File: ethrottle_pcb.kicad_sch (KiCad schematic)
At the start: 57 parts, among them J1 ATM15-08PA-BM02, Q1 ZXTR2105F-7, U1 MCP6004, U2 MCP6004, U3 MCP6004, U4 UB2-5NUN

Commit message: finished routing
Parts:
- H1, H2, H3, H4: footprint (none) -> MountingHole:MountingHole_3.5mm_Pad
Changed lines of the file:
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@@
       (effects (font (size 1.27 1.27)) (justify left))
     )
-    (property "Footprint" "" (id 2) (at 241.3 27.94 0)
+    (property "Footprint" "MountingHole:MountingHole_3.5mm_Pad" (id 2) (at 241.3 27.94 0)
       (effects (font (size 1.27 1.27)) hide)
     )
@@
       (effects (font (size 1.27 1.27)) (justify left))
     )
-    (property "Footprint" "" (id 2) (at 237.49 27.94 0)
+    (property "Footprint" "MountingHole:MountingHole_3.5mm_Pad" (id 2) (at 237.49 27.94 0)
       (effects (font (size 1.27 1.27)) hide)
     )
@@
       (effects (font (size 1.27 1.27)) (justify left))
     )
-    (property "Footprint" "" (id 2) (at 233.68 27.94 0)
+    (property "Footprint" "MountingHole:MountingHole_3.5mm_Pad" (id 2) (at 233.68 27.94 0)
       (effects (font (size 1.27 1.27)) hide)
     )
@@
       (effects (font (size 1.27 1.27)) (justify left))
     )
-    (property "Footprint" "" (id 2) (at 245.11 27.94 0)
+    (property "Footprint" "MountingHole:MountingHole_3.5mm_Pad" (id 2) (at 245.11 27.94 0)
       (effects (font (size 1.27 1.27)) hide)
     )
@@
     )
     (path "/c86d50f5-711f-4a3c-a410-cabcde07bdde"
-      (reference "H1") (unit 1) (value "MountingHole_Pad") (footprint "")
+      (reference "H1") (unit 1) (value "MountingHole_Pad") (footprint "MountingHole:MountingHole_3.5mm_Pad")
     )
     (path "/9a5cb1a6-f24b-4474-afa2-0fecffe0198e"
-      (reference "H2") (unit 1) (value "MountingHole_Pad") (footprint "")
+      (reference "H2") (unit 1) (value "MountingHole_Pad") (footprint "MountingHole:MountingHole_3.5mm_Pad")
     )
     (path "/47b0c02d-82c1-43cd-8381-8e6ee286c3ef"
-      (reference "H3") (unit 1) (value "MountingHole_Pad") (footprint "")
+      (reference "H3") (unit 1) (value "MountingHole_Pad") (footprint "MountingHole:MountingHole_3.5mm_Pad")
     )
     (path "/e2c40712-e7d7-45b4-872b-410fde8473b9"
-      (reference "H4") (unit 1) (value "MountingHole_Pad") (footprint "")
+      (reference "H4") (unit 1) (value "MountingHole_Pad") (footprint "MountingHole:MountingHole_3.5mm_Pad")
     )
     (path "/4f0316f3-2f03-4993-a8a1-815407511b62"

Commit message: layout edits
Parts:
- added TP1: TREF-Test, TestPoint:TestPoint_Plated_Hole_D2.0mm, symbol Connector:TestPoint
- added TP2: BREF-Test, TestPoint:TestPoint_Plated_Hole_D2.0mm, symbol Connector:TestPoint
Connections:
- net BREF: now also TP2.1
- net TREF: now also TP1.1
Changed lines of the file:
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@@
   (junction (at 62.23 66.04) (diameter 0) (color 0 0 0 0)
   )
+  (junction (at 69.85 52.07) (diameter 0) (color 0 0 0 0)
+  )
+  (junction (at 69.85 71.12) (diameter 0) (color 0 0 0 0)
+  )
   (wire (pts (xy 160.02 60.96) (xy 166.37 60.96))
     (stroke (width 0) (type default) (color 0 0 0 0))
@@
     (stroke (width 0) (type default) (color 0 0 0 0))
   )
+  (wire (pts (xy 64.77 66.04) (xy 73.66 66.04))
+    (stroke (width 0) (type default) (color 0 0 0 0))
+  )
   (wire (pts (xy 100.33 90.17) (xy 114.3 90.17))
     (stroke (width 0) (type default) (color 0 0 0 0))
@@
     (stroke (width 0) (type default) (color 0 0 0 0))
   )
+  (wire (pts (xy 59.69 71.12) (xy 69.85 71.12))
+    (stroke (width 0) (type default) (color 0 0 0 0))
+  )
   (wire (pts (xy 270.51 93.98) (xy 270.51 86.36))
     (stroke (width 0) (type default) (color 0 0 0 0))
@@
     (stroke (width 0) (type default) (color 0 0 0 0))
   )
+  (wire (pts (xy 69.85 52.07) (xy 73.66 52.07))
+    (stroke (width 0) (type default) (color 0 0 0 0))
+  )
   (wire (pts (xy 59.69 66.04) (xy 62.23 66.04))
     (stroke (width 0) (type default) (color 0 0 0 0))
@@
     (stroke (width 0) (type default) (color 0 0 0 0))
   )
-  (wire (pts (xy 64.77 66.04) (xy 73.66 66.04))
-    (stroke (width 0) (type default) (color 0 0 0 0))
-  )
   (wire (pts (xy 222.25 99.06) (xy 227.33 99.06))
     (stroke (width 0) (type default) (color 0 0 0 0))
   )
+  (wire (pts (xy 64.77 52.07) (xy 69.85 52.07))
+    (stroke (width 0) (type default) (color 0 0 0 0))
+  )
   (wire (pts (xy 271.78 101.6) (xy 267.97 101.6))
     (stroke (width 0) (type default) (color 0 0 0 0))
@@
   )
   (wire (pts (xy 223.52 113.03) (xy 271.78 113.03))
+    (stroke (width 0) (type default) (color 0 0 0 0))
+  )
+  (wire (pts (xy 69.85 71.12) (xy 73.66 71.12))
     (stroke (width 0) (type default) (color 0 0 0 0))
   )
@@
     )
   )
-  (global_label "BREF" (shape input) (at 73.66 71.12 180) (fields_autoplaced)
+  (global_label "BREF" (shape input) (at 59.69 71.12 180) (fields_autoplaced)
     (effects (font (size 1.27 1.27)) (justify right))
-    (property "Intersheet References" "${INTERSHEET_REFS}" (id 0) (at 66.4693 71.1994 0)
+    (property "Intersheet References" "${INTERSHEET_REFS}" (id 0) (at 52.4993 71.1994 0)
       (effects (font (size 1.27 1.27)) (justify right) hide)
     )
@@
     )
   )
-  (global_label "TREF" (shape input) (at 73.66 52.07 180) (fields_autoplaced)
+  (global_label "TREF" (shape input) (at 64.77 52.07 180) (fields_autoplaced)
     (effects (font (size 1.27 1.27)) (justify right))
-    (property "Intersheet References" "${INTERSHEET_REFS}" (id 0) (at 66.7717 52.1494 0)
+    (property "Intersheet References" "${INTERSHEET_REFS}" (id 0) (at 57.8817 52.1494 0)
       (effects (font (size 1.27 1.27)) (justify right) hide)
     )
@@
     (pin "1")
   )
+  (symbol (lib_id "Connector:TestPoint") (at 69.85 52.07 180) (unit 1)
+    (in_bom yes) (on_board yes)
+    (property "Reference" "TP1" (id 0) (at 69.85 49.53 0)
+      (effects (font (size 1.27 1.27)) (justify right))
+    )
+    (property "Value" "TREF-Test" (id 1) (at 72.39 63.5 90)
+      (effects (font (size 1.27 1.27)) (justify right))
+    )
+    (property "Footprint" "TestPoint:TestPoint_Plated_Hole_D2.0mm" (id 2) (at 64.77 52.07 0)
+      (effects (font (size 1.27 1.27)) hide)
+    )
+    (property "Datasheet" "~" (id 3) (at 64.77 52.07 0)
+      (effects (font (size 1.27 1.27)) hide)
+    )
+    (pin "1")
+  )
   (symbol (lib_id "Amplifier_Operational:MCP6004") (at 214.63 143.51 0) (unit 5)
     (in_bom yes) (on_board yes)
@@
     (pin "1")
   )
+  (symbol (lib_id "Connector:TestPoint") (at 69.85 71.12 180) (unit 1)
+    (in_bom yes) (on_board yes)
+    (property "Reference" "TP2" (id 0) (at 71.12 73.66 0)
+      (effects (font (size 1.27 1.27)) (justify right))
+    )
+    (property "Value" "BREF-Test" (id 1) (at 72.39 85.09 90)
+      (effects (font (size 1.27 1.27)) (justify right))
+    )
+    (property "Footprint" "TestPoint:TestPoint_Plated_Hole_D2.0mm" (id 2) (at 64.77 71.12 0)
+      (effects (font (size 1.27 1.27)) hide)
+    )
+    (property "Datasheet" "~" (id 3) (at 64.77 71.12 0)
+      (effects (font (size 1.27 1.27)) hide)
+    )
+    (pin "1")
+  )
   (symbol (lib_id "power:GND") (at 179.07 151.13 0) (unit 1)
     (in_bom yes) (on_board yes) (fields_autoplaced)
@@
       (reference "R26") (unit 1) (value "1k") (footprint "Resistor_SMD:R_01005_0402Metric")
     )
+    (path "/0f398a6b-70fb-4a4d-8c4d-409df7e390fd"
+      (reference "TP1") (unit 1) (value "TREF-Test") (footprint "TestPoint:TestPoint_Plated_Hole_D2.0mm")
+    )
+    (path "/3a6f3c75-f7a5-4176-9d15-a707551bc0d9"
+      (reference "TP2") (unit 1) (value "BREF-Test") (footprint "TestPoint:TestPoint_Plated_Hole_D2.0mm")
+    )
     (path "/f0df9610-d7e0-45ea-82a7-3deb1fb5d694"

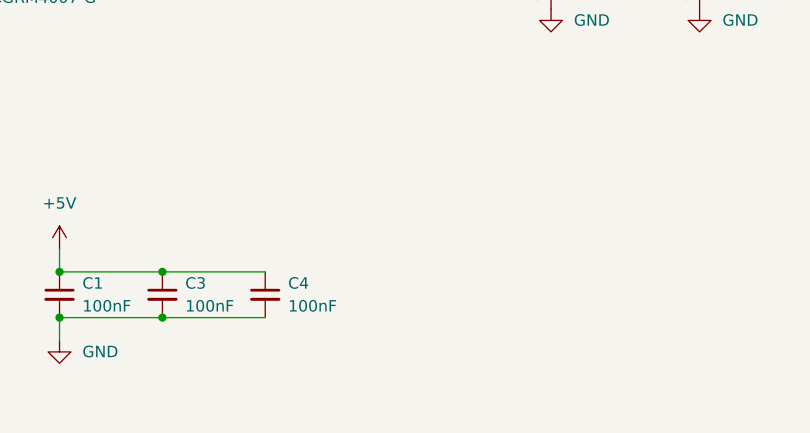
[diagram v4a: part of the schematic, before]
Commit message: add decoupling capacitor
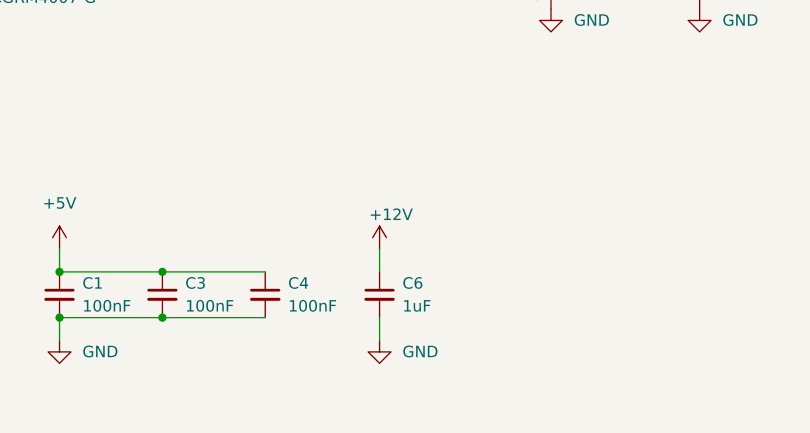
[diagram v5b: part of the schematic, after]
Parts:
- added C6: 1uF, Capacitor_SMD:C_0201_0603Metric, symbol Device:C_Small
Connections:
- net +12V: now also C6.1
- net GND: now also C6.2
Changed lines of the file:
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@@
+    (stroke (width 0) (type default) (color 0 0 0 0))
+  )
+  (wire (pts (xy 160.02 185.42) (xy 160.02 187.96))
     (stroke (width 0) (type default) (color 0 0 0 0))
   )
@@
   )
   (wire (pts (xy 57.15 133.35) (xy 62.23 133.35))
+    (stroke (width 0) (type default) (color 0 0 0 0))
+  )
+  (wire (pts (xy 160.02 177.8) (xy 160.02 180.34))
     (stroke (width 0) (type default) (color 0 0 0 0))
   )
@@
     (pin "2")
   )
+  (symbol (lib_id "power:GND") (at 160.02 187.96 0) (unit 1)
+    (in_bom yes) (on_board yes) (fields_autoplaced)
+    (property "Reference" "#PWR051" (id 0) (at 160.02 194.31 0)
+      (effects (font (size 1.27 1.27)) hide)
+    )
+    (property "Value" "GND" (id 1) (at 162.56 189.2299 0)
+      (effects (font (size 1.27 1.27)) (justify left))
+    )
+    (property "Footprint" "" (id 2) (at 160.02 187.96 0)
+      (effects (font (size 1.27 1.27)) hide)
+    )
+    (property "Datasheet" "" (id 3) (at 160.02 187.96 0)
+      (effects (font (size 1.27 1.27)) hide)
+    )
+    (pin "1")
+  )
   (symbol (lib_id "power:GND") (at 124.46 187.96 0) (unit 1)
     (in_bom yes) (on_board yes) (fields_autoplaced)
@@
     (pin "1")
     (pin "2")
+  )
+  (symbol (lib_id "power:+12V") (at 160.02 177.8 0) (unit 1)
+    (in_bom yes) (on_board yes)
+    (property "Reference" "#PWR050" (id 0) (at 160.02 181.61 0)
+      (effects (font (size 1.27 1.27)) hide)
+    )
+    (property "Value" "+12V" (id 1) (at 161.29 173.99 0))
+    (property "Footprint" "" (id 2) (at 160.02 177.8 0)
+      (effects (font (size 1.27 1.27)) hide)
+    )
+    (property "Datasheet" "" (id 3) (at 160.02 177.8 0)
+      (effects (font (size 1.27 1.27)) hide)
+    )
+    (pin "1")
   )
   (symbol (lib_id "power:PWR_FLAG") (at 97.79 182.88 0) (unit 1)
@@
     (pin "2")
   )
+  (symbol (lib_id "Device:C_Small") (at 160.02 182.88 0) (unit 1)
+    (in_bom yes) (on_board yes) (fields_autoplaced)
+    (property "Reference" "C6" (id 0) (at 162.56 181.6162 0)
+      (effects (font (size 1.27 1.27)) (justify left))
+    )
+    (property "Value" "1uF" (id 1) (at 162.56 184.1562 0)
+      (effects (font (size 1.27 1.27)) (justify left))
+    )
+    (property "Footprint" "Capacitor_SMD:C_0201_0603Metric" (id 2) (at 160.02 182.88 0)
+      (effects (font (size 1.27 1.27)) hide)
+    )
+    (property "Datasheet" "https://search.murata.co.jp/Ceramy/image/img/A01X/G101/ENG/GRM033R60J105MEA2-02.pdf" (id 3) (at 160.02 182.88 0)
+      (effects (font (size 1.27 1.27)) hide)
+    )
+    (pin "1")
+    (pin "2")
+  )
   (symbol (lib_id "Amplifier_Operational:MCP6004") (at 173.99 58.42 0) (unit 2)
     (in_bom yes) (on_board yes) (fields_autoplaced)
@@
       (reference "#PWR049") (unit 1) (value "+12V") (footprint "")
     )
+    (path "/3e99151b-271e-4b50-af12-3cf637629ce9"
+      (reference "#PWR050") (unit 1) (value "+12V") (footprint "")
+    )
+    (path "/32e28533-9f5b-4d98-8a95-d6c101584a0e"
+      (reference "#PWR051") (unit 1) (value "GND") (footprint "")
+    )
     (path "/1b640f29-3d5f-434a-b351-9c2d1cc03452"
       (reference "C1") (unit 1) (value "100nF") (footprint "Capacitor_SMD:C_0201_0603Metric")
@@
       (reference "C5") (unit 1) (value "10uF") (footprint "Capacitor_SMD:C_0805_2012Metric")
     )
+    (path "/bd515c98-1462-4b1d-bef4-56a57db1aee7"
+      (reference "C6") (unit 1) (value "1uF") (footprint "Capacitor_SMD:C_0201_0603Metric")
+    )
     (path "/cd943169-25c5-42dc-b71b-d2aa00184062"

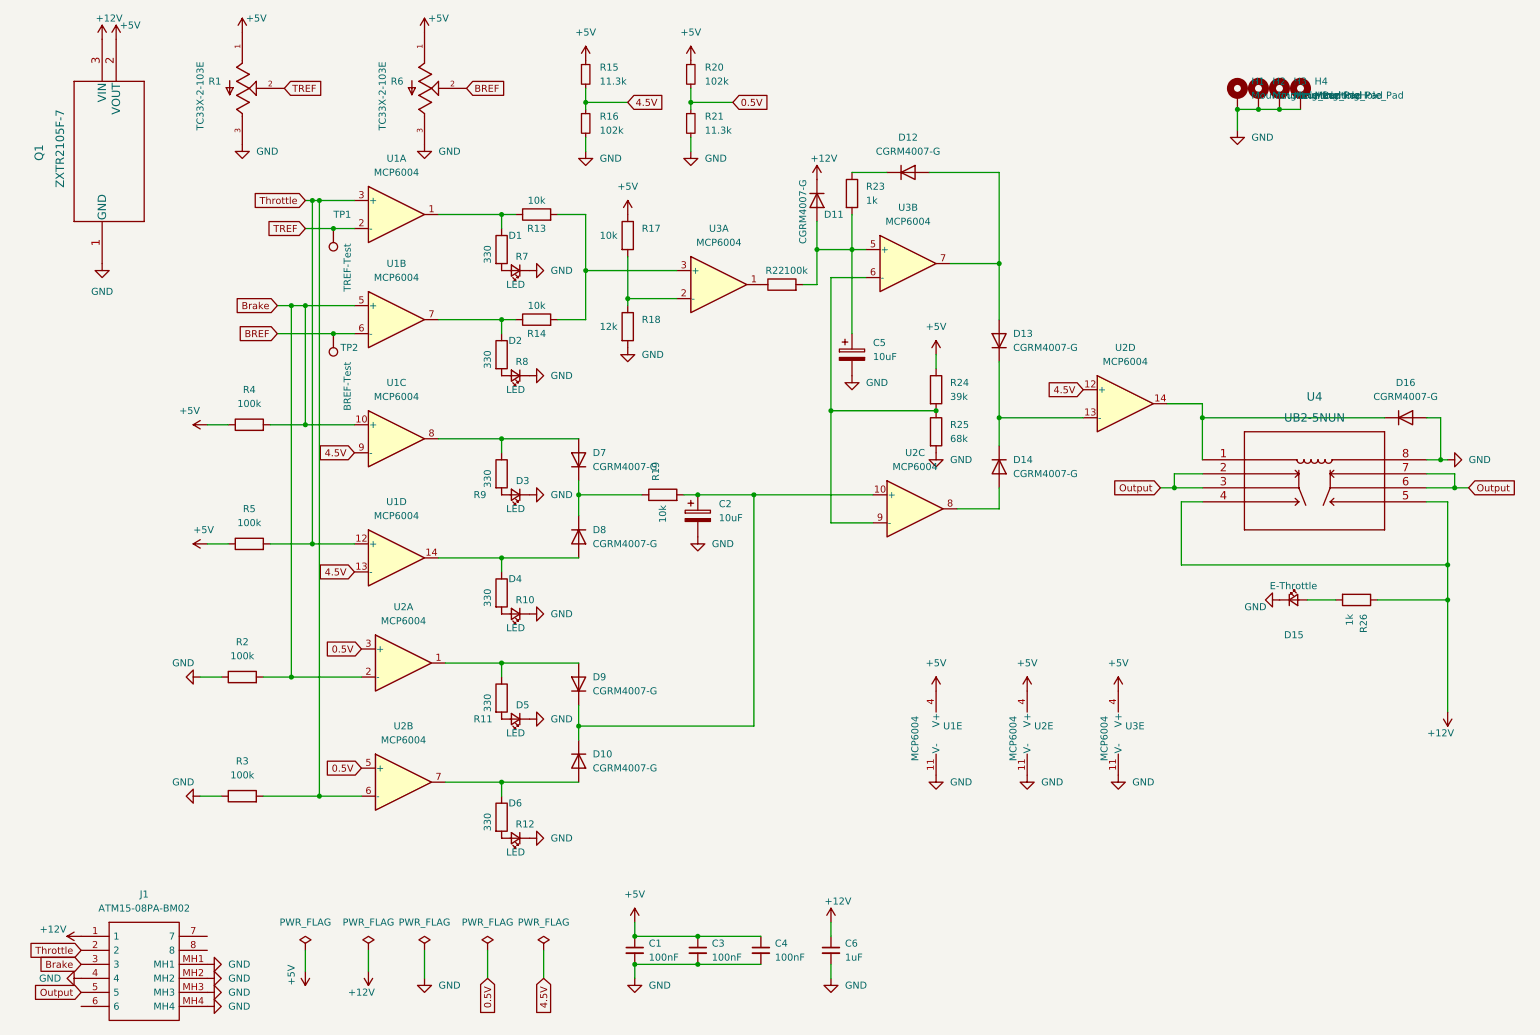
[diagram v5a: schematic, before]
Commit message: change d11 to 5v from 12v, add bjt for relay, lots of layout changes
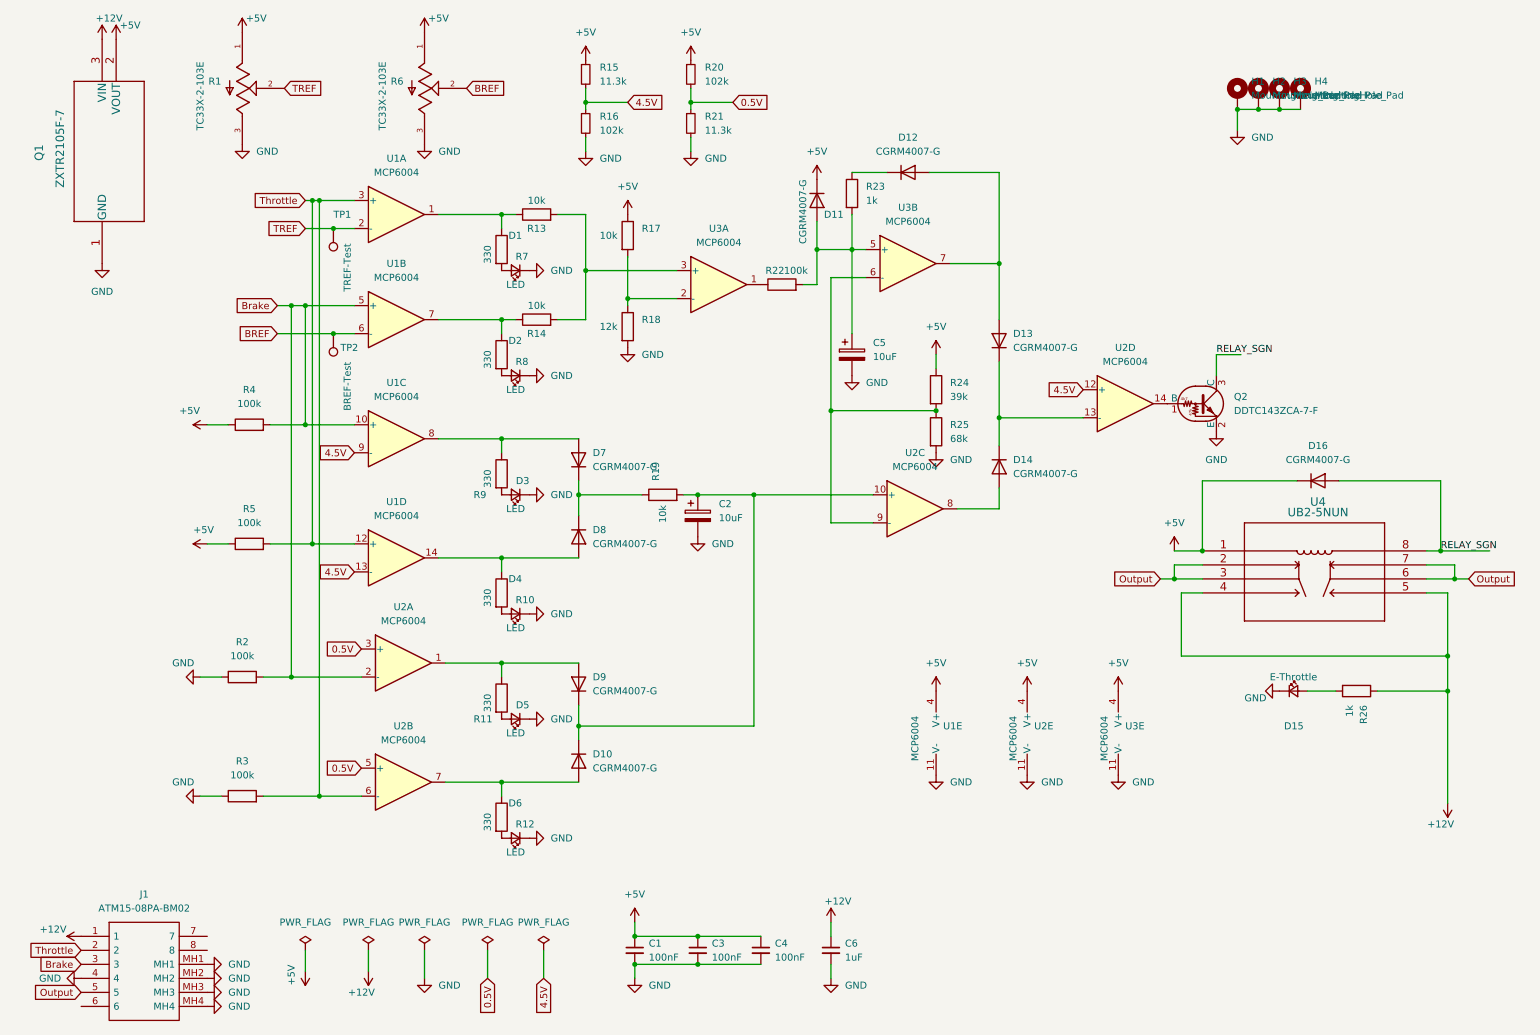
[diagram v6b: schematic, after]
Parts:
- added Q2: DDTC143ZCA-7-F, Package_TO_SOT_SMD:SOT-23, symbol Transistor_BJT:DTC143Z
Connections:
- net +12V: no longer D11.1 (K)
- net +5V: now also D11.1 (K), D16.1 (K), U4.1
- net GND: now also Q2.2 (E); no longer D16.2 (A), U4.8
- new net: Q2.1 (B), U2.14
- new net RELAY_SGN: D16.2 (A), Q2.3 (C), U4.8
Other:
- moved on the sheet: D15, D16, R26, U4

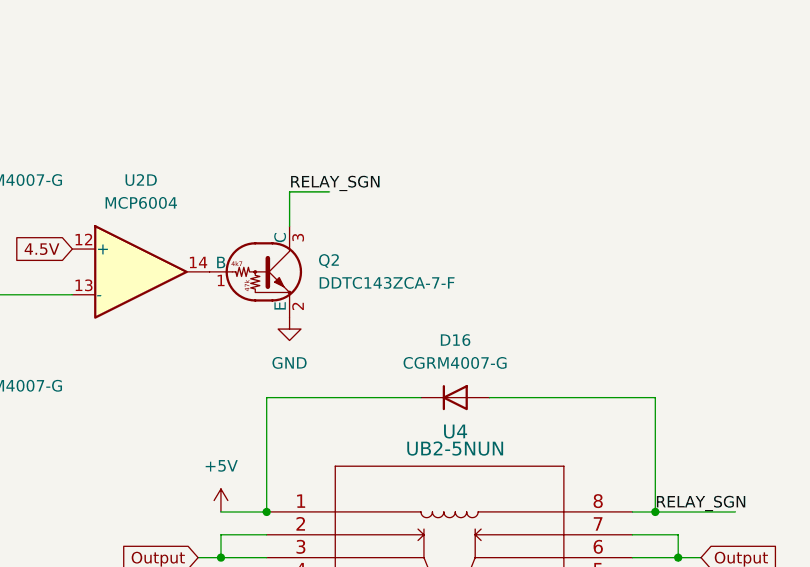
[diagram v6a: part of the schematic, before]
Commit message: move relay to bottom, increase 12v rail trace thickness, various ancillary layout changes
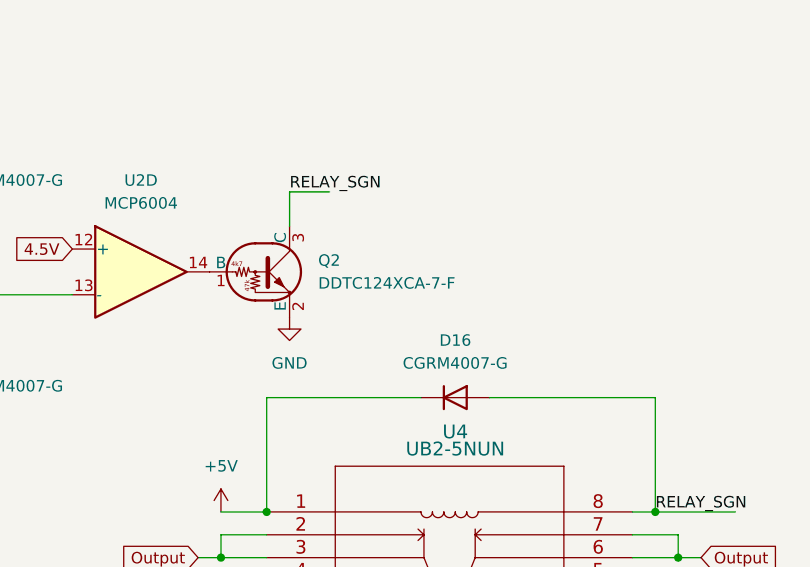
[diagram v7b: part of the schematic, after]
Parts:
- Q2: value DDTC143ZCA-7-F -> DDTC124XCA-7-F
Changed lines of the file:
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@@
       (effects (font (size 1.27 1.27)) (justify left))
     )
-    (property "Value" "DDTC143ZCA-7-F" (id 1) (at 233.045 85.0899 0)
+    (property "Value" "DDTC124XCA-7-F" (id 1) (at 233.045 85.0899 0)
       (effects (font (size 1.27 1.27)) (justify left))
     )
@@
     )
     (path "/0fabc74a-1641-4d25-816f-64e9c3a94164"
-      (reference "Q2") (unit 1) (value "DDTC143ZCA-7-F") (footprint "Package_TO_SOT_SMD:SOT-23")
+      (reference "Q2") (unit 1) (value "DDTC124XCA-7-F") (footprint "Package_TO_SOT_SMD:SOT-23")
     )
     (path "/9abae127-e0ee-46b2-b6e2-dbc096437d9a"
